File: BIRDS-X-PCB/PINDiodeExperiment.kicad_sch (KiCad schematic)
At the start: 21 parts, among them Q1 MMBF4392LT1G, U1 LM358DR

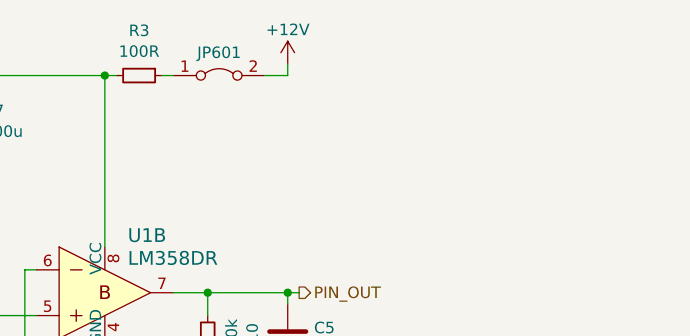
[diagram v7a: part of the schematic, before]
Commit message: Refactor jumper for PIN experiment power
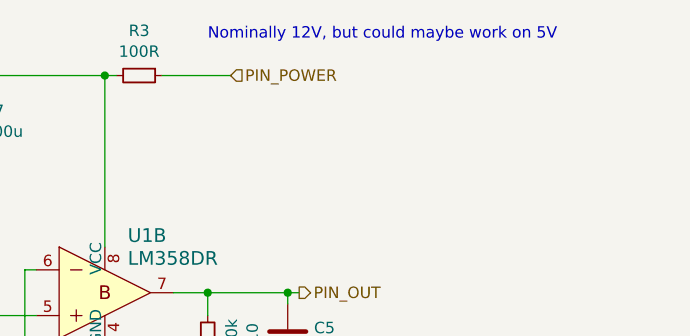
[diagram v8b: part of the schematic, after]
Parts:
- removed JP601: Jumper_2_Bridged, Jumper:SolderJumper-2_P1.3mm_Open_RoundedPad1.0x1.5mm, symbol Jumper:Jumper_2_Bridged
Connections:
- net PIN_POWER: now reaches R3.1
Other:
- note added: "Nominally 12V, but could maybe work on 5V"
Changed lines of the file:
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@@
-    (stroke (width 0) (type default))
-  )
-  (wire (pts (xy 180.34 63.5) (xy 182.88 63.5))
     (stroke (width 0) (type default))
   )
@@
     (stroke (width 0) (type default))
   )
-  (wire (pts (xy 168.91 63.5) (xy 170.18 63.5))
+  (wire (pts (xy 168.91 63.5) (xy 176.53 63.5))
     (stroke (width 0) (type default))
   )
@@
     (stroke (width 0) (type default))
   )
-  (wire (pts (xy 182.88 63.5) (xy 182.88 62.23))
-    (stroke (width 0) (type default))
-  )
   (wire (pts (xy 173.99 87.63) (xy 173.99 90.17))
     (stroke (width 0) (type default))
@@
   (wire (pts (xy 73.66 63.5) (xy 82.55 63.5))
     (stroke (width 0) (type default))
+  )
+  (text "Nominally 12V, but could maybe work on 5V" (at 173.99 59.69 0)
+    (effects (font (size 1.27 1.27)) (justify left bottom))
   )
   (hierarchical_label "PIN_OUT" (shape output) (at 184.15 87.63 0) (fields_autoplaced)
     (effects (font (size 1.27 1.27)) (justify left))
   )
-  (symbol (lib_id "power:+12V") (at 182.88 62.23 0) (unit 1)
-    (in_bom yes) (on_board yes) (dnp no)
-    (property "Reference" "#PWR0607" (at 182.88 66.04 0)
-      (effects (font (size 1.27 1.27)) hide)
-    )
-    (property "Value" "+12V" (at 182.88 58.42 0)
-      (effects (font (size 1.27 1.27)))
-    )
-    (property "Footprint" "" (at 182.88 62.23 0)
-      (effects (font (size 1.27 1.27)) hide)
-    )
-    (property "Datasheet" "" (at 182.88 62.23 0)
-      (effects (font (size 1.27 1.27)) hide)
-    )
-    (pin "1")
-    (instances
-      (project "BIRDS-X-PCB"
-        (path "/c2796b15-795a-4d6e-ad4b-0ba87ded4bc9/69450ea3-1431-409d-8bc6-7752e7bc3ab3"
-          (reference "#PWR0607") (unit 1)
-        )
-        (path "/c2796b15-795a-4d6e-ad4b-0ba87ded4bc9/24de0e99-26aa-4106-b99d-2d4b1437b640"
-          (reference "#PWR0704") (unit 1)
-        )
-        (path "/c2796b15-795a-4d6e-ad4b-0ba87ded4bc9/20e9fdd9-b39a-4397-9a05-a4dbf181acd2"
-          (reference "#PWR0804") (unit 1)
-        )
-        (path "/c2796b15-795a-4d6e-ad4b-0ba87ded4bc9/004149c1-7266-4be8-8957-13aaab4479fd"
-          (reference "#PWR0904") (unit 1)
-        )
-      )
-    )
+  (hierarchical_label "PIN_POWER" (shape input) (at 176.53 63.5 0) (fields_autoplaced)
+    (effects (font (size 1.27 1.27)) (justify left))
   )
   (symbol (lib_id "Device:C") (at 137.16 114.3 0) (unit 1)
@@
         )
       )
-    )
-  )
-  (symbol (lib_id "Jumper:Jumper_2_Bridged") (at 175.26 63.5 0) (unit 1)
-    (in_bom yes) (on_board yes) (dnp no)
-    (property "Reference" "JP601" (at 175.26 60.96 0)
-      (effects (font (size 1.27 1.27)))
-    )
-    (property "Value" "Jumper_2_Bridged" (at 175.26 60.96 0)
-      (effects (font (size 1.27 1.27)) hide)
-    )
-    (property "Footprint" "Jumper:SolderJumper-2_P1.3mm_Open_RoundedPad1.0x1.5mm" (at 175.26 63.5 0)
-      (effects (font (size 1.27 1.27)) hide)
-    )
-    (property "Datasheet" "~" (at 175.26 63.5 0)
-      (effects (font (size 1.27 1.27)) hide)
-    )
-    (pin "1")
-    (pin "2")
-    (instances
-      (project "BIRDS-X-PCB"
-        (path "/c2796b15-795a-4d6e-ad4b-0ba87ded4bc9/69450ea3-1431-409d-8bc6-7752e7bc3ab3"
-          (reference "JP601") (unit 1)
-        )
-        (path "/c2796b15-795a-4d6e-ad4b-0ba87ded4bc9/24de0e99-26aa-4106-b99d-2d4b1437b640"
-          (reference "JP701") (unit 1)
-        )
-        (path "/c2796b15-795a-4d6e-ad4b-0ba87ded4bc9/20e9fdd9-b39a-4397-9a05-a4dbf181acd2"
-          (reference "JP801") (unit 1)
-        )
-        (path "/c2796b15-795a-4d6e-ad4b-0ba87ded4bc9/004149c1-7266-4be8-8957-13aaab4479fd"
-          (reference "JP901") (unit 1)
-        )
-      )
